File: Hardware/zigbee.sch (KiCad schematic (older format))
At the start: 15 parts, among them J1 DB9, K1 CONN_3, P1 CONN_4, U1 LM1117, U2 ZIGBEE_XL, U3 LM1117, U4 MAX232

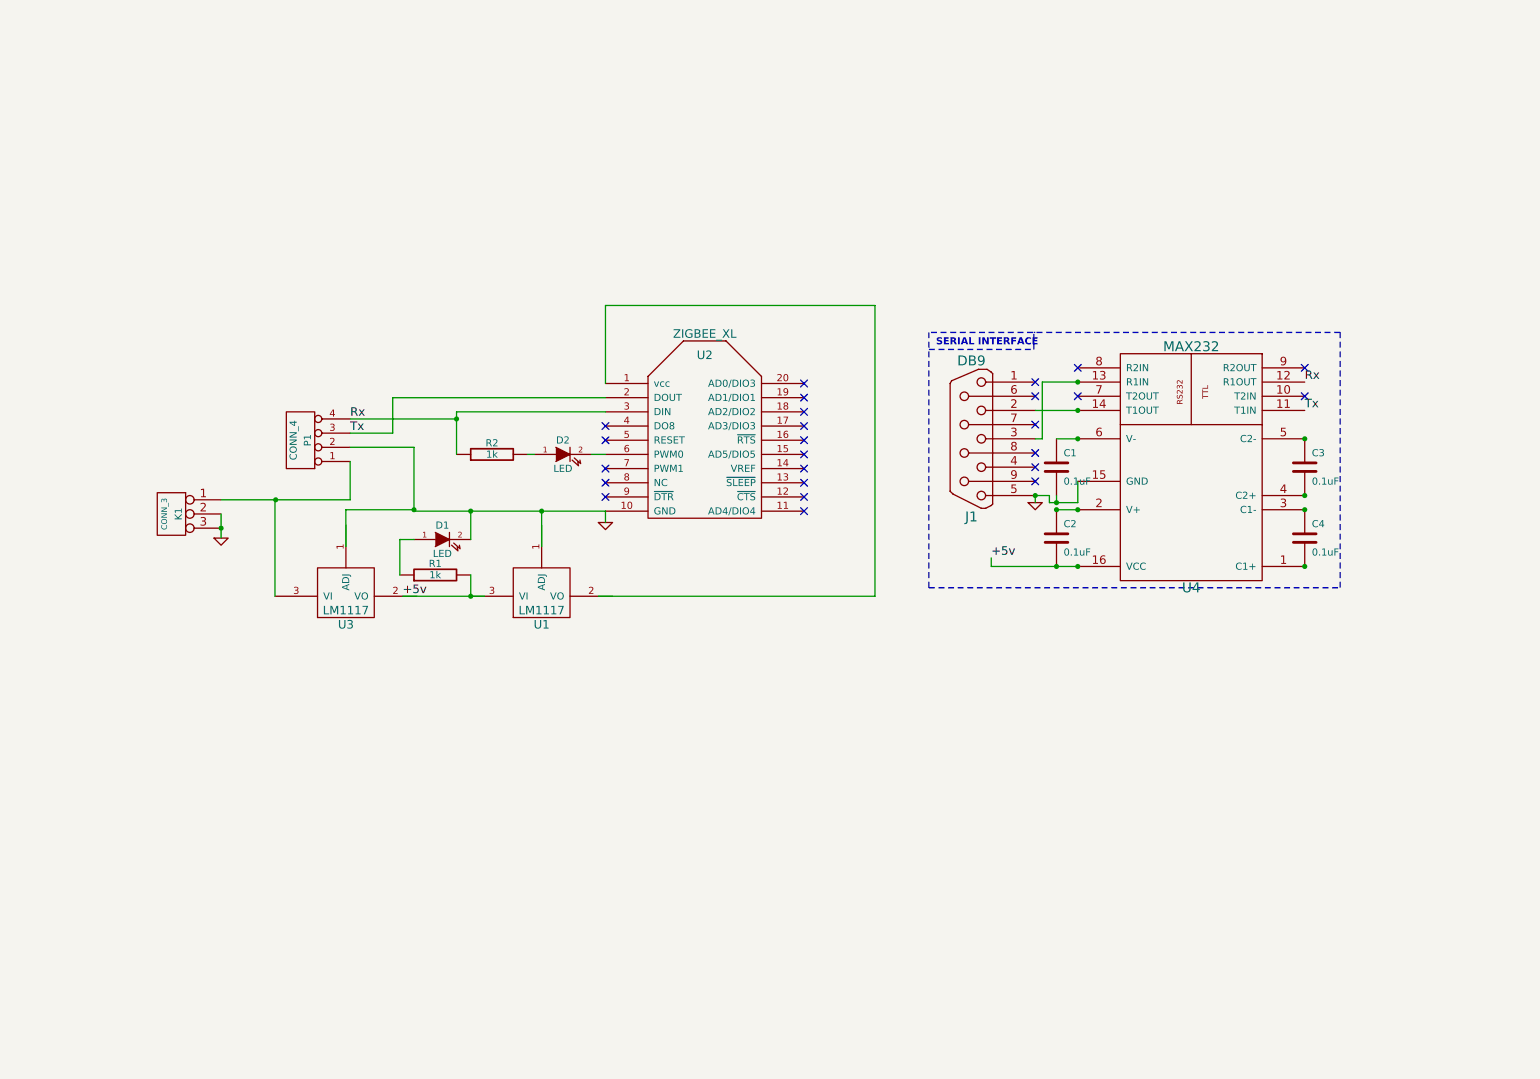
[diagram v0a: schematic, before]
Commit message: beautified Schematic for site upload
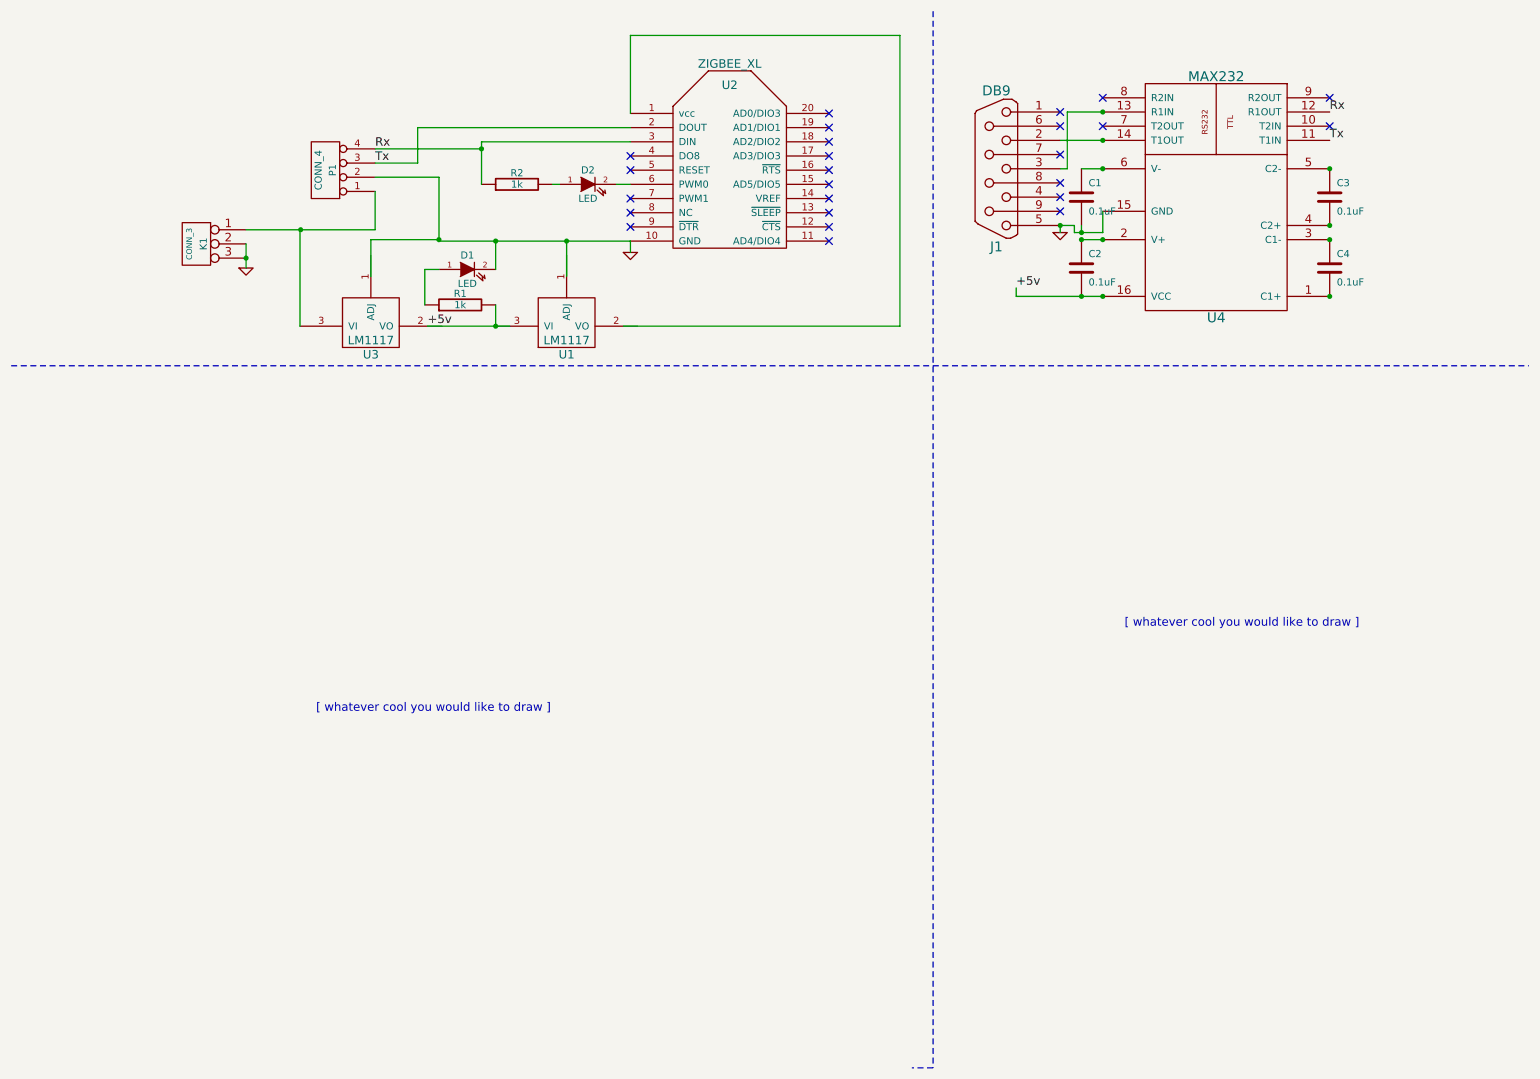
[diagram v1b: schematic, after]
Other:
- note added: "[ whatever cool you would like to draw ]"
- note removed: "SERIAL INTERFACE\n"
- moved on the sheet: C1, C2, C3, C4, D1, D2, J1, K1, P1, R1, R2, U1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
